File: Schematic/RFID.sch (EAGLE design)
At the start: 6 parts, among them U1 HTRC11001T/02EE,11

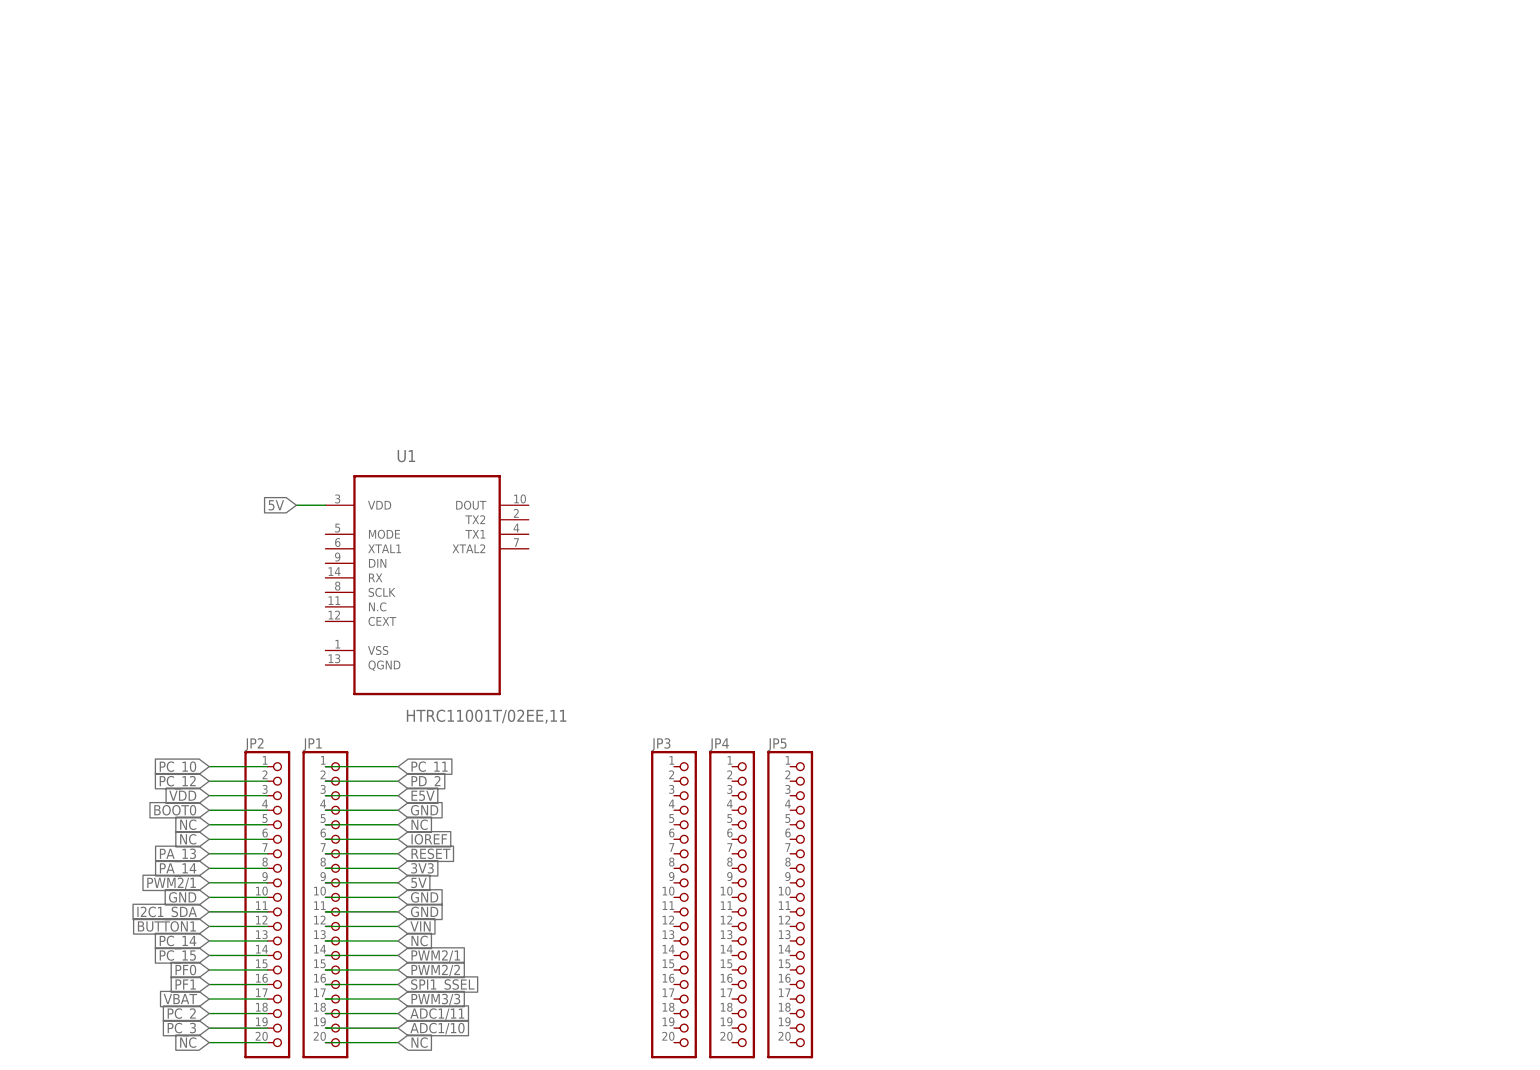
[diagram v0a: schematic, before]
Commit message: IC Connections, STM32 Pins
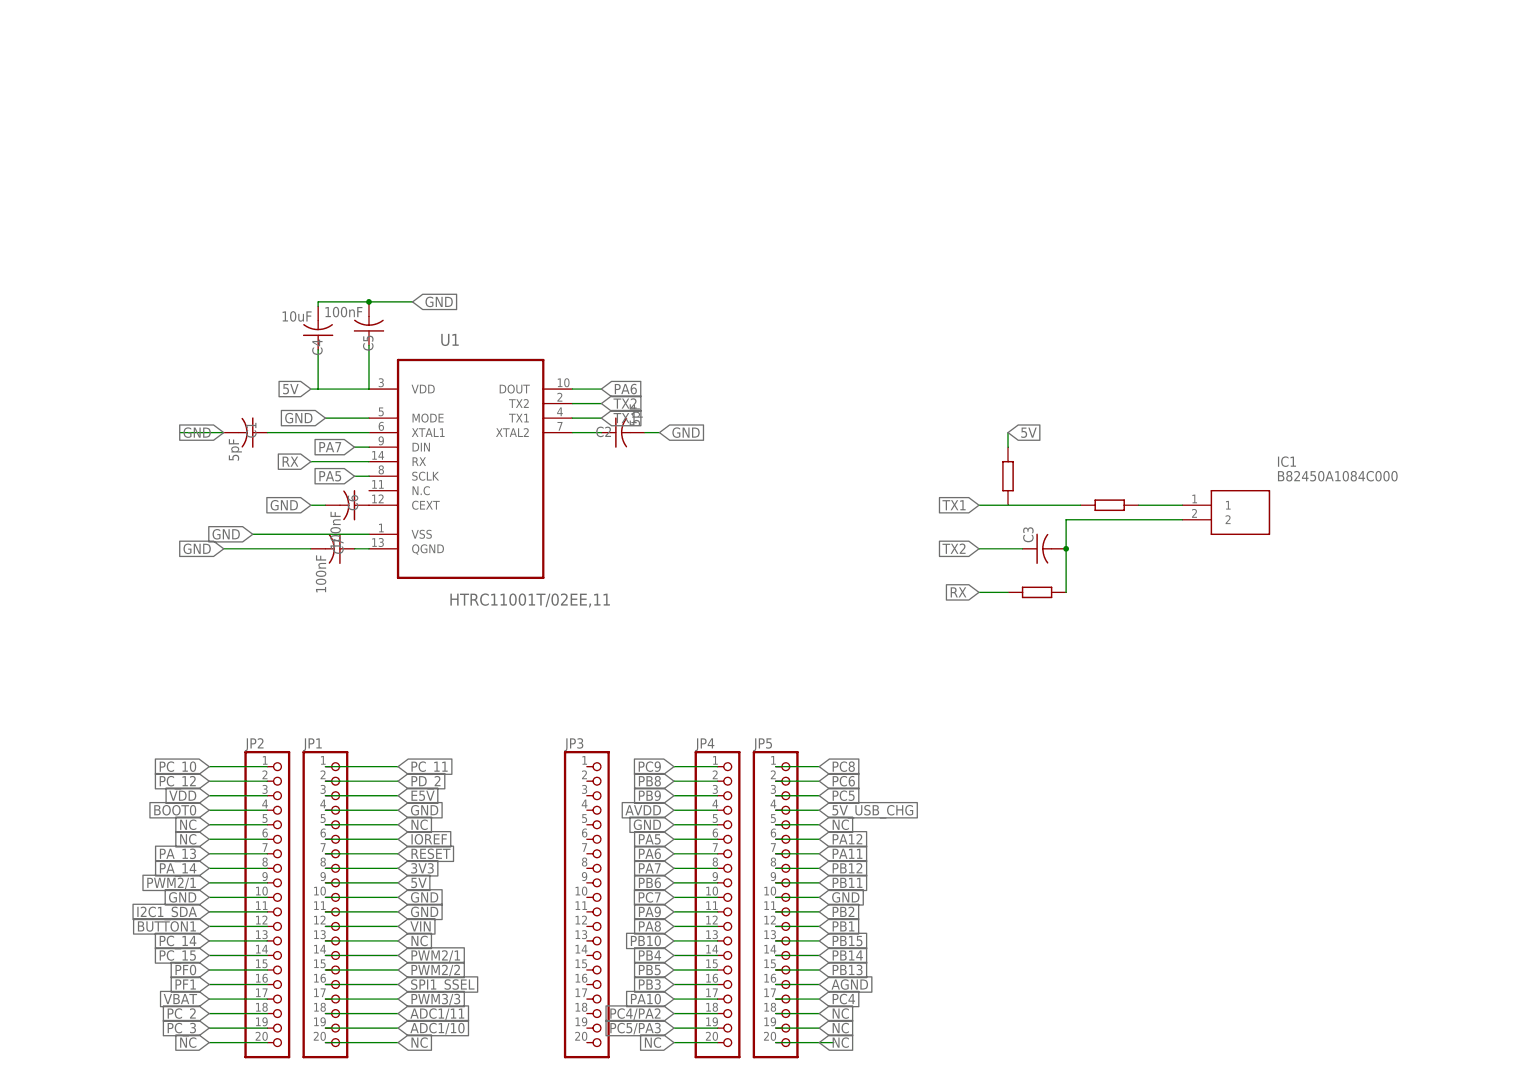
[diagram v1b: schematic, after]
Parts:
- added C1, C2: 5pF, rcl:C-USC0805
- added C3: (no value), rcl:C-USC0805
- added C4: 10uF, rcl:C-USC0805
- added C5, C6, C7: 100nF, rcl:C-USC0805
- added IC1: B82450A1084C000, B82450A1084C000:B82450A1084C000
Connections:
- new net 5V_USB_CHG: JP5.4
- new net AGND: JP5.16
- new net ANT1: IC1.1
- new net ANT2: C3.2, IC1.2
- new net AVDD: JP4.4
- new net N$6: C1.1, U1.XTAL1
- new net N$7: C2.1, U1.XTAL2
- new net N$8: C6.1, U1.CEXT
- new net N$9: C7.1, U1.QGND
- new net PA10: JP4.17
- new net PA11: JP5.7
- new net PA12: JP5.6
- new net PA5: JP4.6, U1.SCLK
- new net PA6: JP4.7, U1.DOUT
- new net PA7: JP4.8, U1.DIN
- new net PA8: JP4.12
- new net PA9: JP4.11
- new net PB1: JP5.12
- new net PB10: JP4.13
- new net PB11: JP5.9
- new net PB12: JP5.8
- new net PB13: JP5.15
- new net PB14: JP5.14
- new net PB15: JP5.13
- new net PB2: JP5.11
- new net PB3: JP4.16
- new net PB4: JP4.14
- new net PB5: JP4.15
- new net PB6: JP4.9
- new net PB8: JP4.2
- new net PB9: JP4.3
- new net PC4: JP5.17
- new net PC4/PA2: JP4.18
- new net PC5: JP5.3
- new net PC5/PA3: JP4.19
- new net PC6: JP5.2
- new net PC7: JP4.10
- new net PC8: JP5.1
- new net PC9: JP4.1
- new net RX: U1.RX
- new net TX1: U1.TX1
- new net TX2: C3.1, U1.TX2
- net 5V: now also C4.1, C5.1
- net GND: now also C1.2, C2.2, C4.2, C5.2, C6.2, C7.2, JP4.5, JP5.10, U1.MODE, U1.VSS
- net NC: now also JP4.20, JP5.18, JP5.19, JP5.20, JP5.5
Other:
- moved on the sheet: JP3, JP4, JP5, U1

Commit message: Aesthetics improved
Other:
- note added: "Antenna Ckt"
- note added: "External Conn + Power supply"
- note added: "Microcontroller circuit"
- note added: "Reader IC"
- moved on the sheet: C1, C2, C3, C4, C5, C6, C7, IC1, JP1, JP2, JP3, JP4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

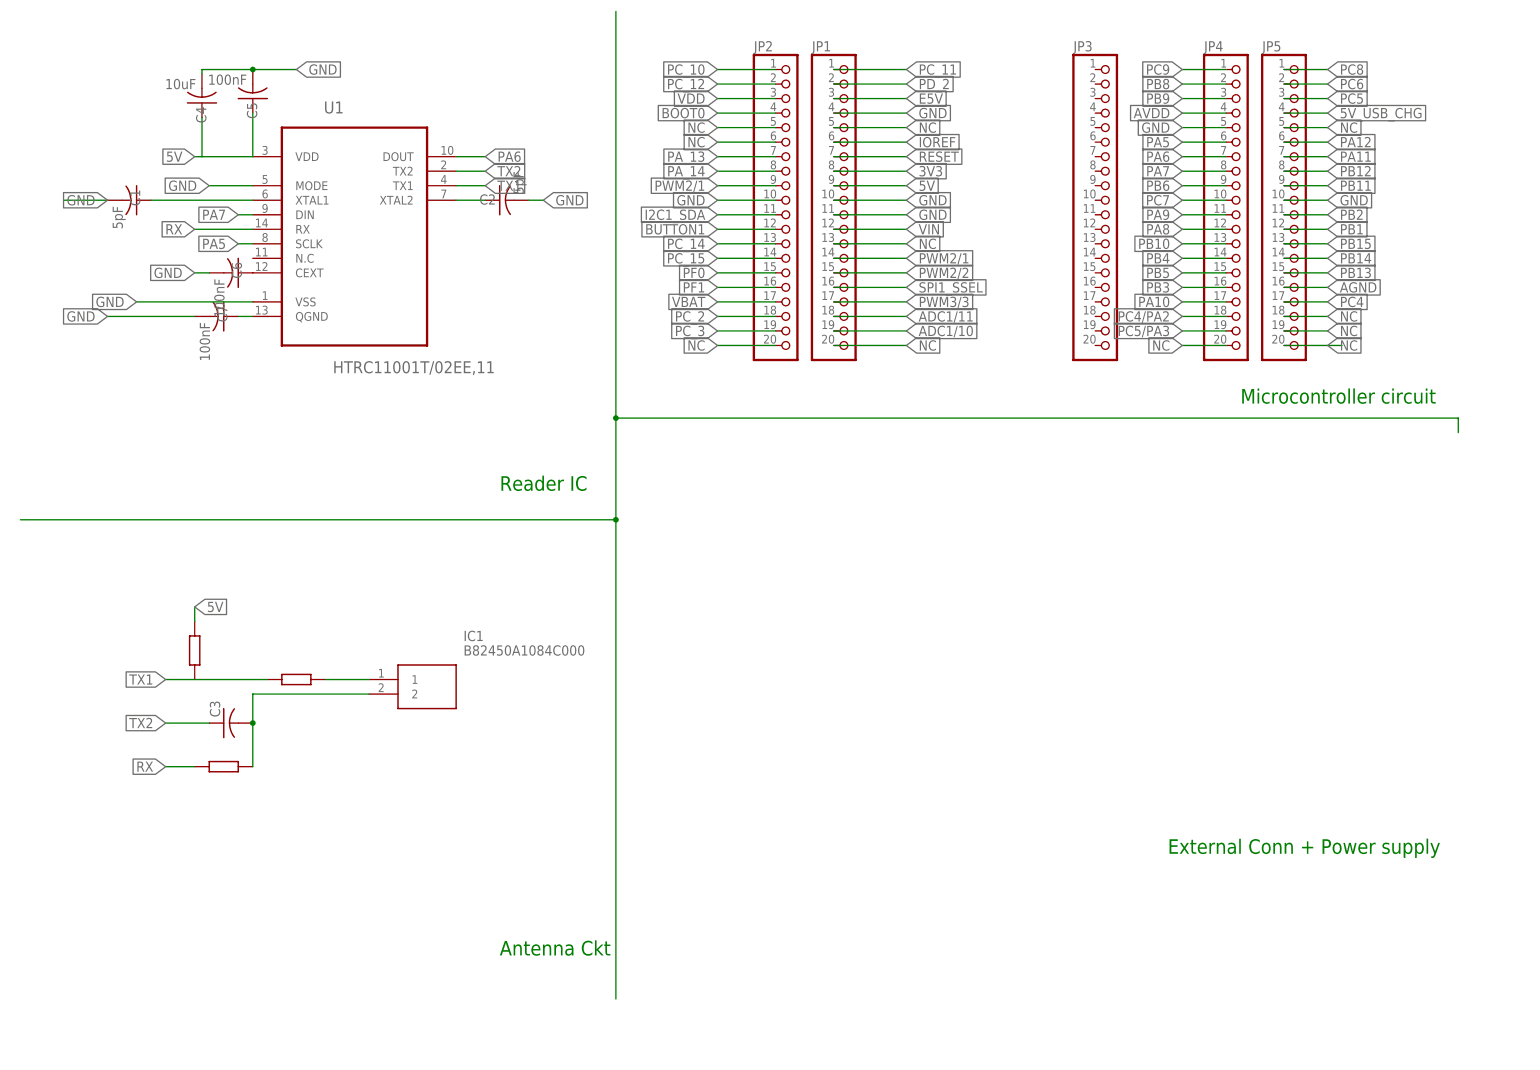
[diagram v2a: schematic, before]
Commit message: Schematic without impedance matching
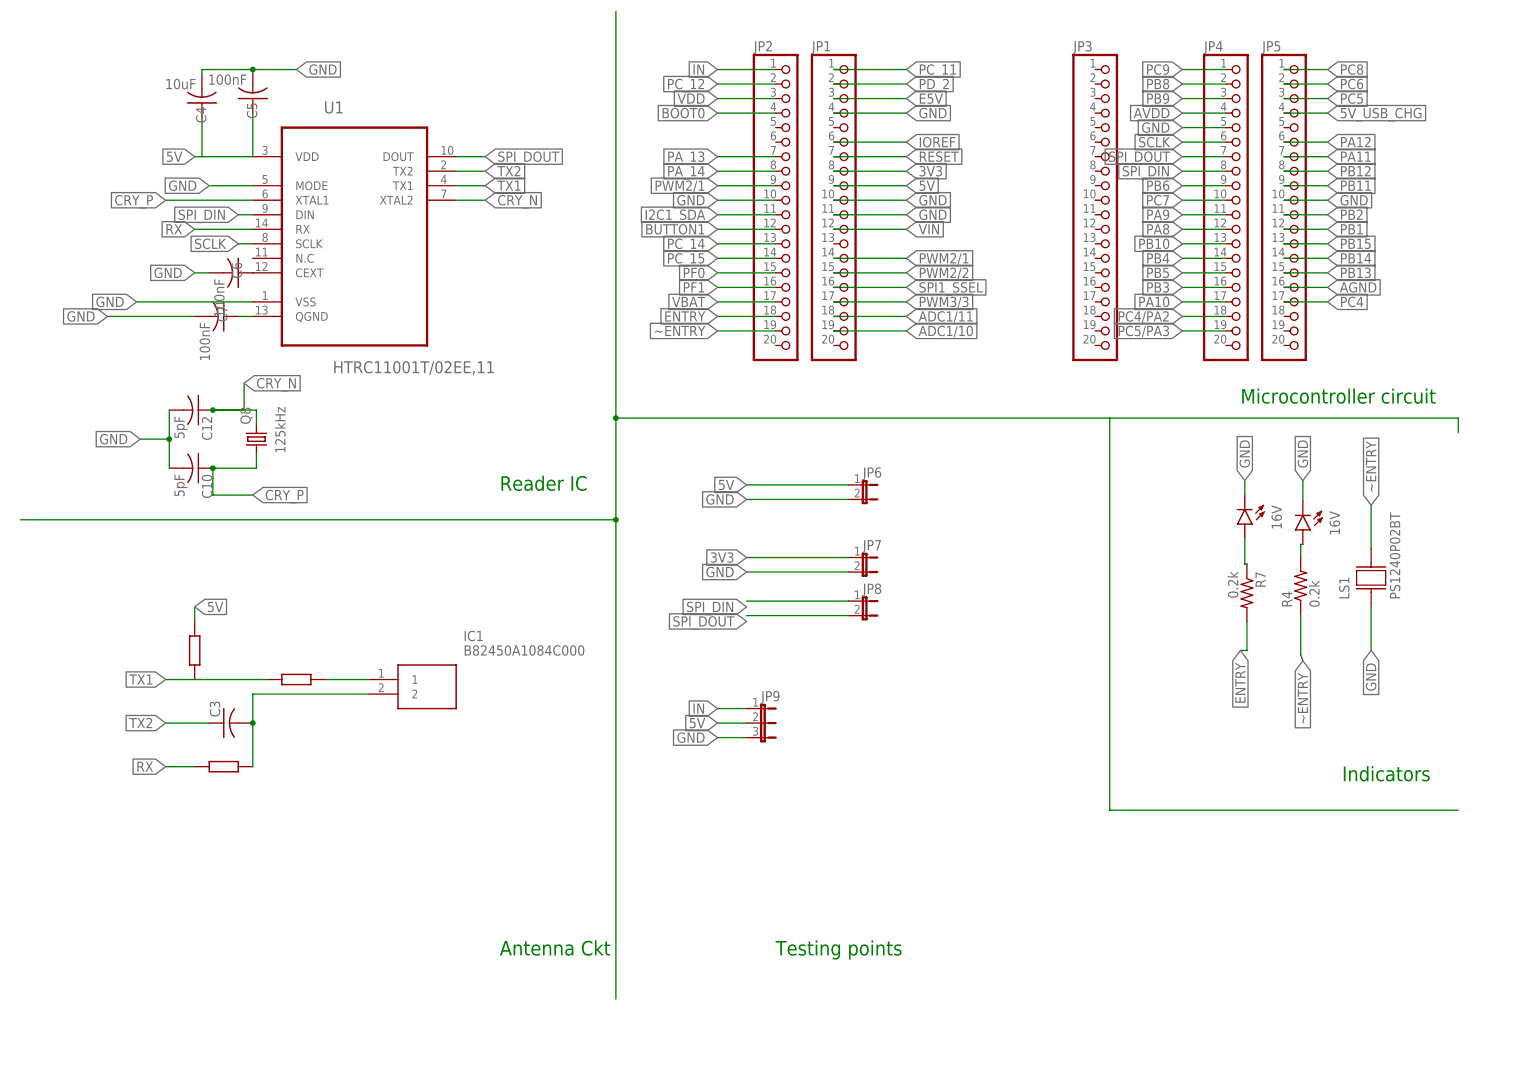
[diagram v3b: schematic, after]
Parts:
- removed C1, C2: 5pF, rcl:C-USC0805
- added C10, C12: 5pF, resistor:C-US025-024X044
- added GPIO_5V, GPIO_POWER: 16V, led:LED5MM
- added JP6, JP7, JP8: (no value), jumper:JP1E
- added JP9: (no value), jumper:JP2E
- added LS1: PS1240P02BT, PS1240P02BT:PS1240P02BT
- added Q8: 125kHz, crystal:CRYSTALHC49S
- added R4, R7: 0.2k, adafruit:R-US_R0603
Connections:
- net PA5 renamed SCLK
- removed net N$6: C1.1, U1.XTAL1
- removed net N$7: C2.1, U1.XTAL2
- removed net NC: JP1.13, JP1.20, JP1.5, JP2.20, JP2.5, JP2.6, JP4.20, JP5.18, JP5.19, JP5.20, JP5.5
- removed net PA6: JP4.7, U1.DOUT
- removed net PA7: JP4.8, U1.DIN
- removed net PC_10: JP2.1
- removed net PC_2: JP2.18
- removed net PC_3: JP2.19
- new net CRY_N: C12.1, Q8.2, U1.XTAL2
- new net CRY_P: C10.1, Q8.1, U1.XTAL1
- new net ENTRY: JP2.18, R7.2
- new net IN: JP2.1, JP9.1
- new net N$2: GPIO_POWER.A, R4.2
- new net N$3: GPIO_5V.A, R7.1
- new net SPI_DIN: JP4.8, JP8.1, U1.DIN
- new net SPI_DOUT: JP4.7, JP8.2, U1.DOUT
- new net ~ENTRY: JP2.19, LS1.2, R4.1
- net 3V3: now also JP7.1
- net 5V: now also JP6.1, JP9.2
- net GND: now also C10.2, C12.2, GPIO_5V.C, GPIO_POWER.C, JP6.2, JP7.2, JP9.3, LS1.1; no longer C1.2, C2.2
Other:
- note added: "Indicators"
- note added: "Testing points"
- note removed: "External Conn + Power supply"
